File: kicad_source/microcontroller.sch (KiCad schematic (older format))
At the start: 23 parts, among them CN1 ARDUINO, CON1 Micro_SDCard, SW1 TAST_VER, SW2 TAST_VER, U5 ESP32_WROOM_32, U6 ATECC608A

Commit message: placed FE310, made first connections
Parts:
- removed CN1: ARDUINO, MODULE_compute:ARDUINO, symbol MODULE_compute:ARDUINO
- removed U5: ESP32_WROOM_32, MODULE_compute:ESP32-WROOM-32, symbol MODULE_compute:ESP32_WROOM_32
- added C? (x5): 100n, capacitors:C_0603, symbol devices:C_0603
- added C?: 10u, capacitors:C_0603, symbol devices:C_0603
- added R?: 100, resistors:R_0603, symbol devices:R_1206
- added U?: FE310-G002, QFN:QFN-48-1EP_6x6mm_P0.4mm_EP4.3x4.3mm, symbol IC_microcontroller_SiFive:FE310-G002
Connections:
- net labels added: +1V8, SPI_CS_DIS
- wire segments 153 -> 184
- no-connect marks 15 -> 7
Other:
- note removed: "all used for \nonboard flash"
- moved on the sheet: C10, C11, C9, R18, R19, R8

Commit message: updated power circuit
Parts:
- removed R11: 0r, resistors:R_0603, symbol devices:R_1206
- removed R20, R21: 330k, resistors:R_0603, symbol devices:R_1206
- removed SW1: TAST_VER, mechanical-switches:WE_430182050816, symbol mechanical-switches:TAST_VER
- added C?: 100n, capacitors:C_0603, symbol devices:C_0603
- added C? (x2): 15p, capacitors:C_0603, symbol devices:C_0603
- added R?: 10k, resistors:R_0603, symbol devices:R_1206
- added R?: 1M, resistors:R_0603, symbol devices:R_1206
- added SW?: TAST_VER, mechanical-switches:WE_430182050816, symbol mechanical-switches:TAST_VER
- added Y?: Crystal_SMD_4Pad, crystals:Crystal_SMD_0603_4Pads, symbol devices:Crystal_SMD_4Pad
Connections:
- net labels added: JTAG_TCK, JTAG_TDI, JTAG_TDO, JTAG_TMS, LED, PLL_AVDD, PLL_AVSS, VDD_CORE_EN, WAKE, XTAL_XI, XTAL_XO
- net labels removed: +BATT, ADC_0, ADC_1, ADC_2, ADC_3, ADC_4, ADC_5, ARDUINO_2, ARDUINO_5, ARDUINO_6, ARDUINO_7, ARDUINO_8, ARDUINO_9, BOOT, DAC_1, DAC_2, SPI_CS_EXT, VCC
- wire segments 184 -> 155
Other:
- note added: "PMU_OUT_1 is not needed?"
- note added: "should work using the \ninternal 32 kHz clock, \nbut connect device"
- moved on the sheet: C13, C9, R8, SW2, U6

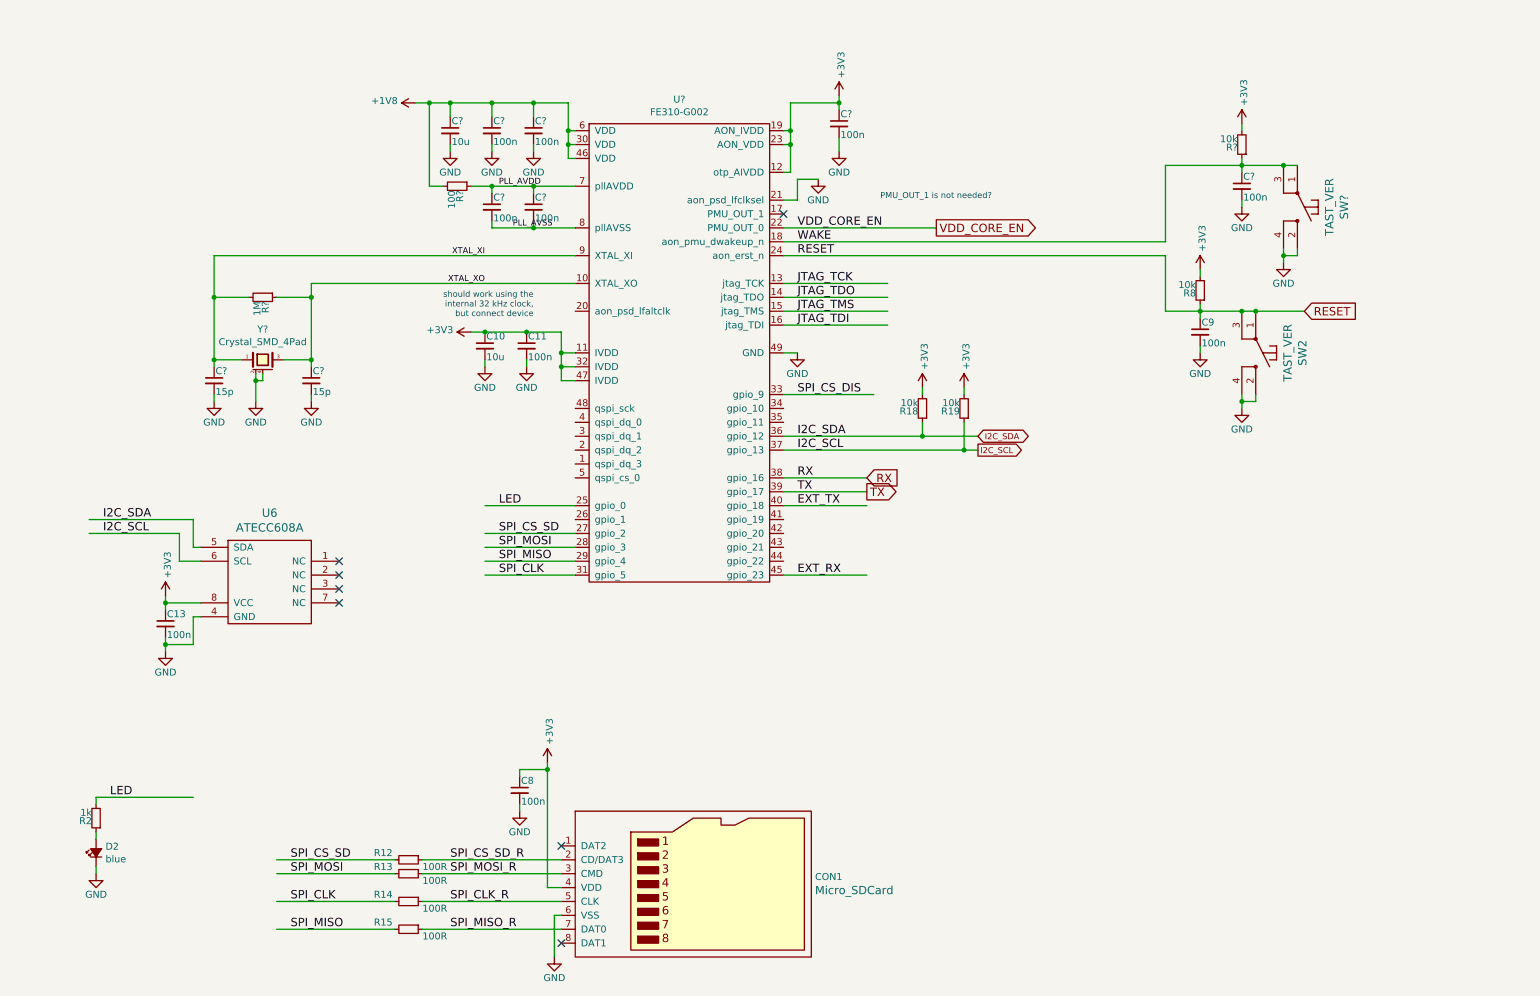
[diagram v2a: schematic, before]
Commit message: added flash, JTAG connector and display to schematic
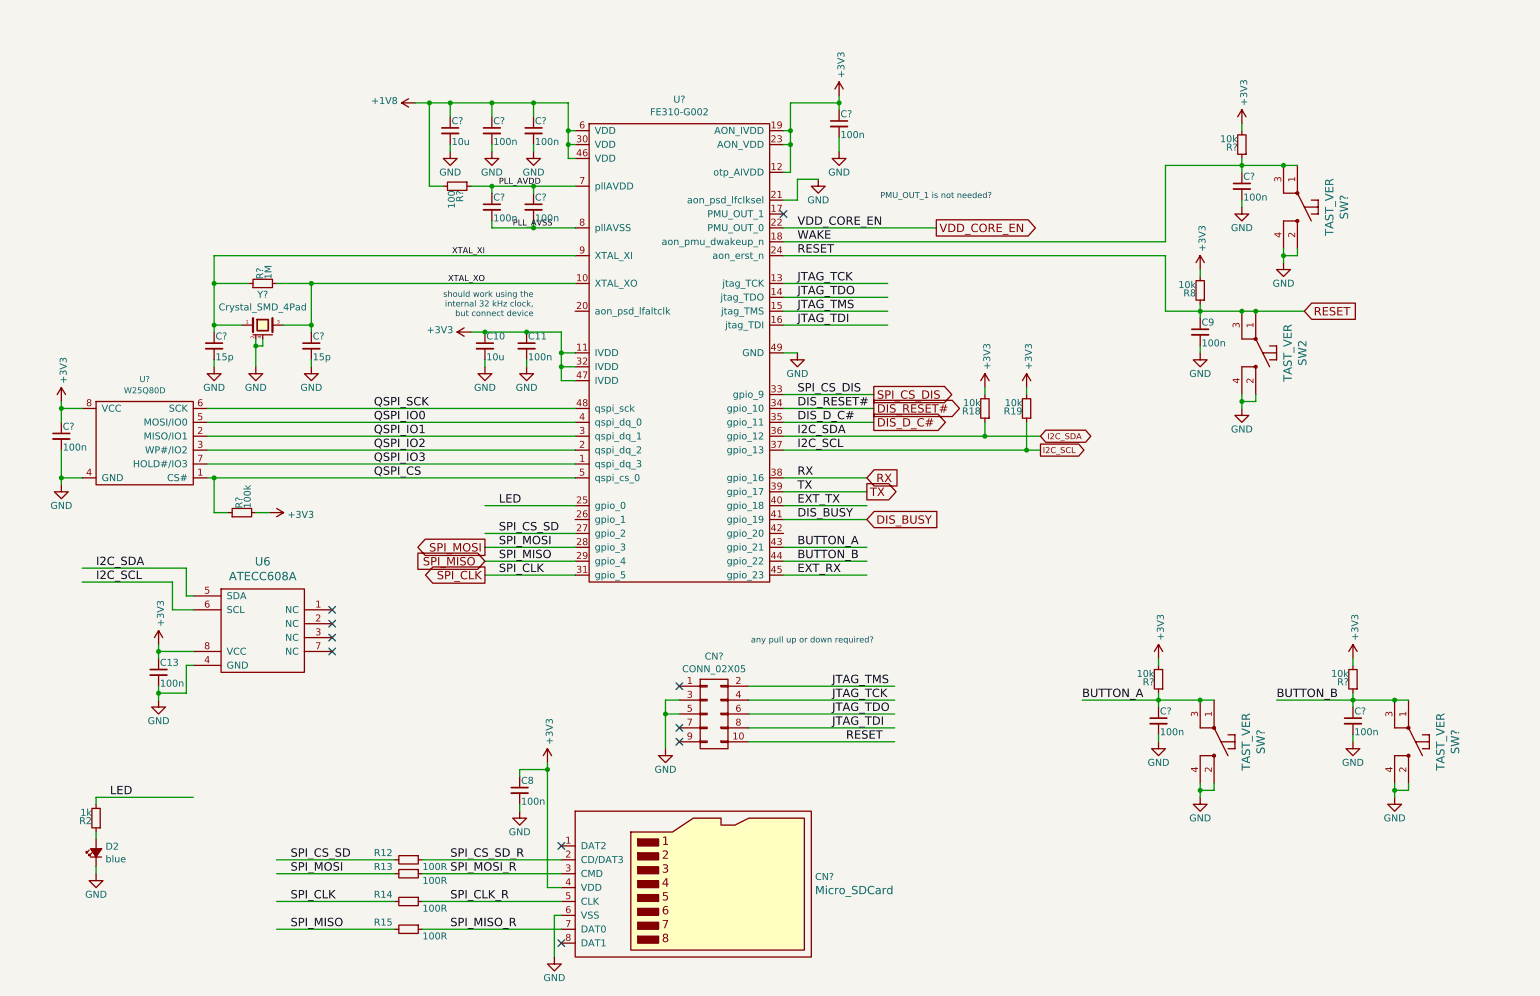
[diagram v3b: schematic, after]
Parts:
- added C? (x3): 100n, capacitors:C_0603, symbol devices:C_0603
- added CN?: CONN_02X05, symbol mechanical-connectors:CONN_02X05
- added R?: 100k, resistors:R_0603, symbol devices:R_1206
- added R? (x2): 10k, resistors:R_0603, symbol devices:R_1206
- added SW? (x2): TAST_VER, mechanical-switches:WE_430182050816, symbol mechanical-switches:TAST_VER
- added U?: W25Q80D, SOIC:SOIC-8_3.9x4.9mm_Pitch1.27mm, symbol IC_memory_flash:W25Q80D
- renumbered CON1 to CN?
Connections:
- net labels added: BUTTON_A, BUTTON_B, DIS_BUSY, DIS_D_C#, DIS_RESET#, QSPI_CS, QSPI_IO0, QSPI_IO1, QSPI_IO2, QSPI_IO3, QSPI_SCK
- wire segments 155 -> 206
- no-connect marks 7 -> 10
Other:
- note added: "any pull up or down required?"
- moved on the sheet: C13, C?, R18, R19, R?, U6, Y?

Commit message: added nfc part, generated schematic pdf
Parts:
- gave numbers to parts that had none: 26
- renumbered C11 to C10, C9 to C15, C13 to C2, C10 to C6, C8 to C9, D2 to D1, R2 to R1, R19 to R10, R8 to R12, R12 to R4, R13 to R5, R14 to R6, R15 to R7, R18 to R9, U6 to U2
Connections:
- net labels added: NFC_BUSY
- wire segments 206 -> 207

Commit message: started placement
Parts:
- CN2: footprint (none) -> pin_headers:Pin_Header_Straight_2x05_Pitch1.27mm
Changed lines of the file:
@@
 F 0 "CN2" H 5600 6015 50  0000 C CNN
 F 1 "CONN_02X05" H 5600 5924 50  0000 C CNN
-F 2 "" H 5600 4400 50  0000 C CNN
+F 2 "pin_headers:Pin_Header_Straight_2x05_Pitch1.27mm" H 5600 4400 50  0000 C CNN
 F 3 "" H 5600 4400 50  0000 C CNN
 	1    5600 5600

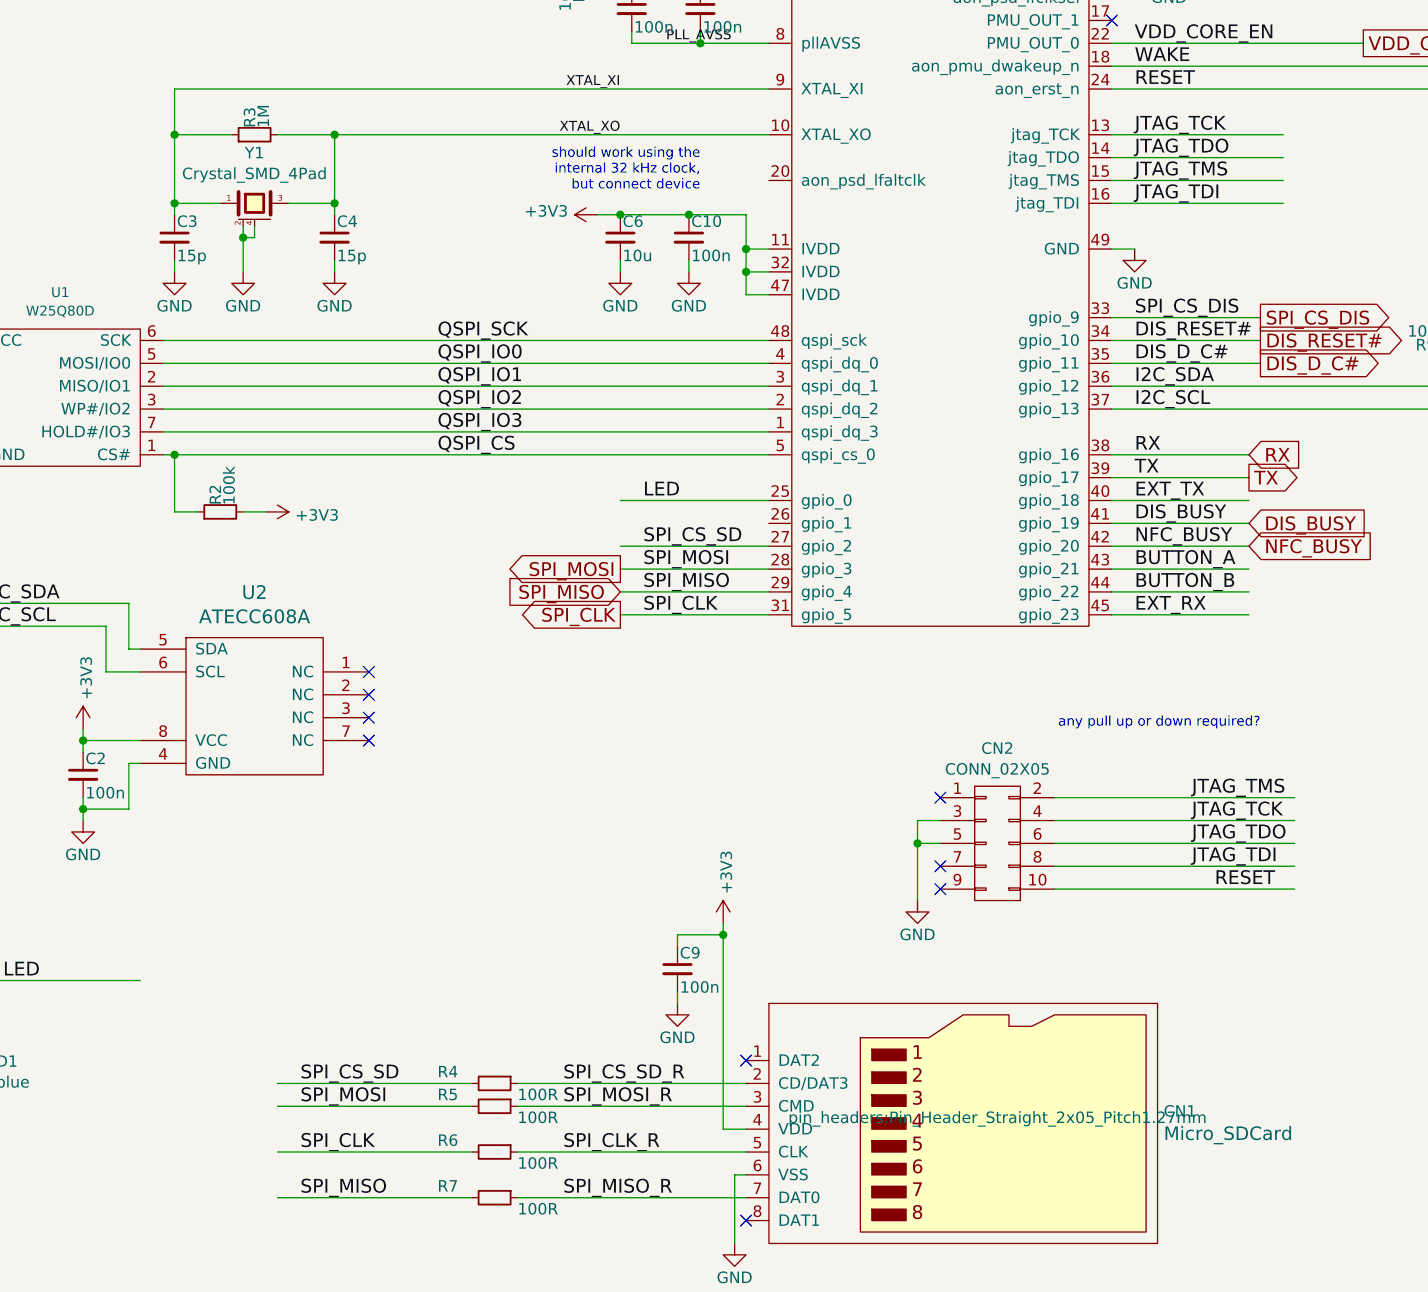
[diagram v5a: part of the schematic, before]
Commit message: added value 16 MHz to crystal, connected pin 1 of CN2 to +3V3
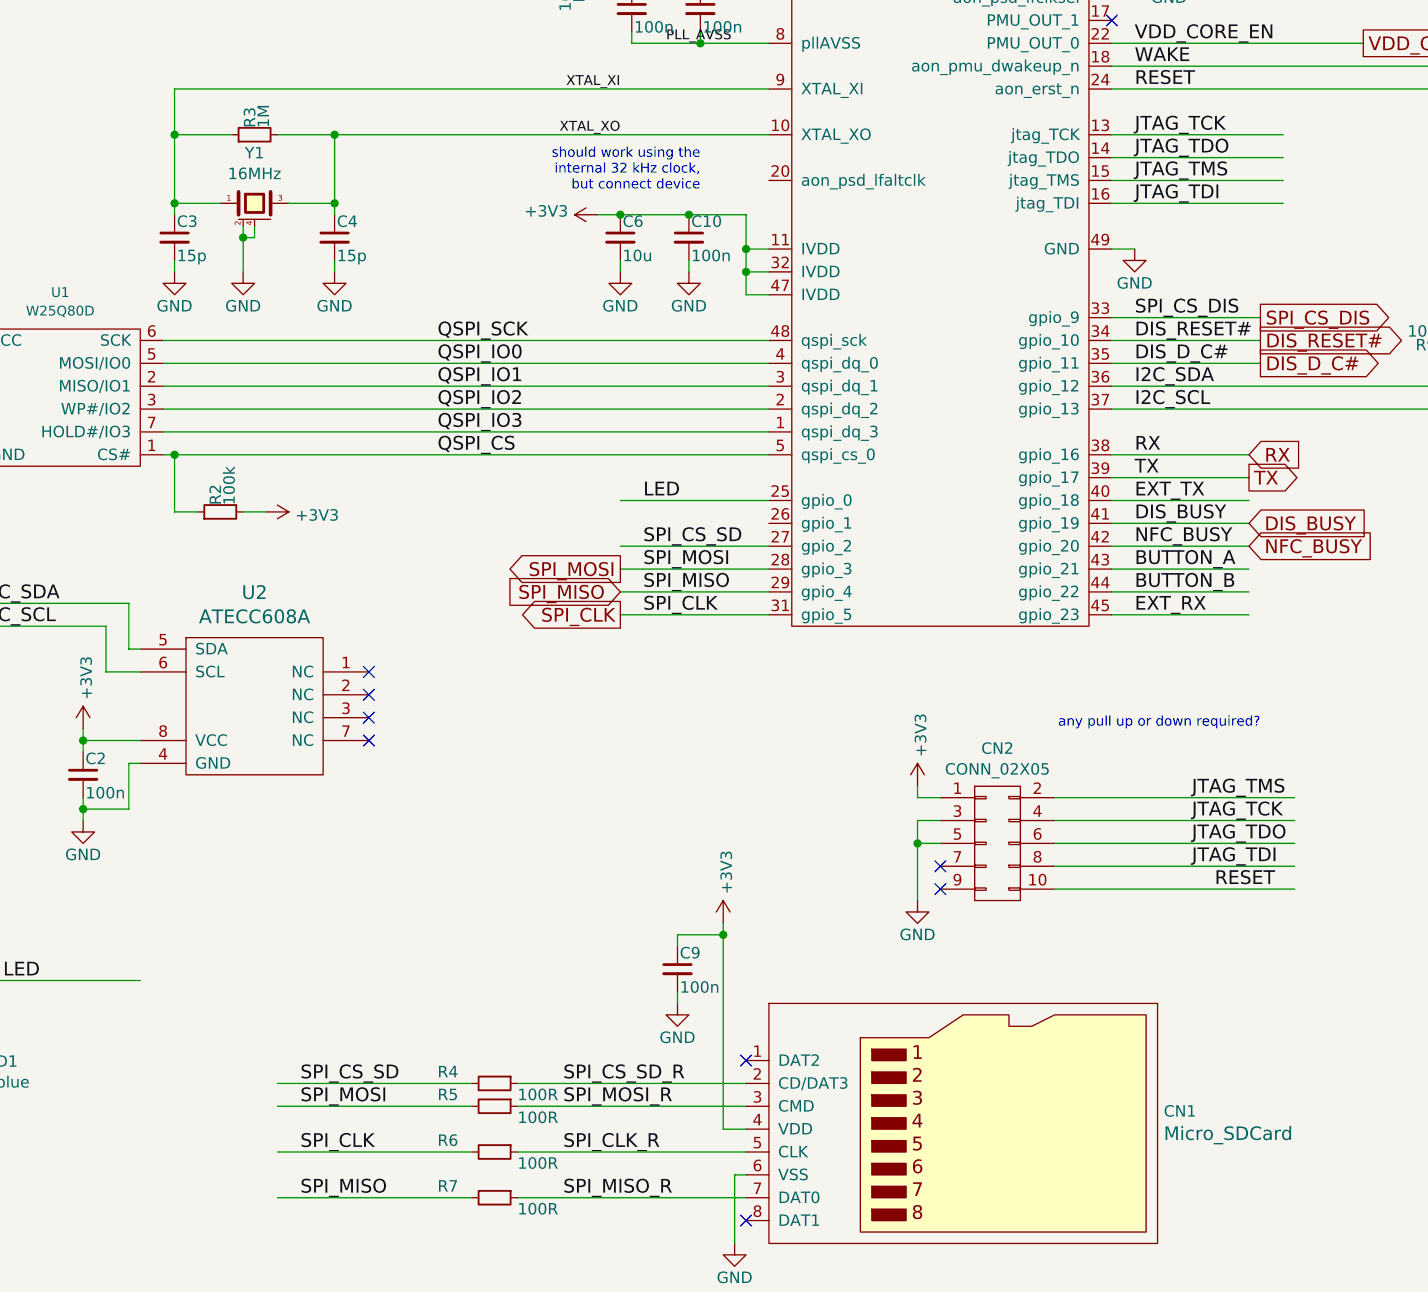
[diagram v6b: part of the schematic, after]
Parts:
- Y1: value Crystal_SMD_4Pad -> 16MHz
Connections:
- wire segments 207 -> 209
- no-connect marks 10 -> 9
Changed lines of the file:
@@
 Sheet 2 7
 Title "Risc V FE310 microcontroller"
-Date "2020-05-10"
+Date "2020-05-13"
 Rev "dev_0.1"
 Comp "generationmake"
@@
 P 2350 2800
 F 0 "Y1" H 2350 3020 50  0000 C CNN
-F 1 "Crystal_SMD_4Pad" H 2350 2929 50  0000 C CNN
+F 1 "16MHz" H 2350 2929 50  0000 C CNN
 F 2 "crystals:Crystal_SMD_0603_4Pads" H 2350 2600 50  0001 C CNN
 F 3 "" H 2350 2800 50  0000 C CNN
@@
 F 0 "CN2" H 5600 6015 50  0000 C CNN
 F 1 "CONN_02X05" H 5600 5924 50  0000 C CNN
-F 2 "pin_headers:Pin_Header_Straight_2x05_Pitch1.27mm" H 5600 4400 50  0000 C CNN
+F 2 "pin_headers:Pin_Header_Straight_2x05_Pitch1.27mm" H 5600 5600 50  0001 C CNN
 F 3 "" H 5600 4400 50  0000 C CNN
 	1    5600 5600
 	1    0    0    -1
 $EndComp
-NoConn ~ 5350 5400
 NoConn ~ 5350 5700
 NoConn ~ 5350 5800
@@
 Text Label 6200 4300 0    60   ~ 0
 NFC_BUSY
+$Comp
+L power-supply:+3V3 #PWR0101
+U 1 1 5EBC2B18
+P 5250 5350
+F 0 "#PWR0101" H 5250 5200 50  0001 C CNN
+F 1 "+3V3" V 5265 5478 50  0000 L CNN
+F 2 "" H 5250 5350 50  0000 C CNN
+F 3 "" H 5250 5350 50  0000 C CNN
+	1    5250 5350
+	1    0    0    -1
+$EndComp
+Wire Wire Line
+	5350 5400 5250 5400
+Wire Wire Line
+	5250 5400 5250 5350
 $EndSCHEMATC
